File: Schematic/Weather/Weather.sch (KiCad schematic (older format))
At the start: 0 parts

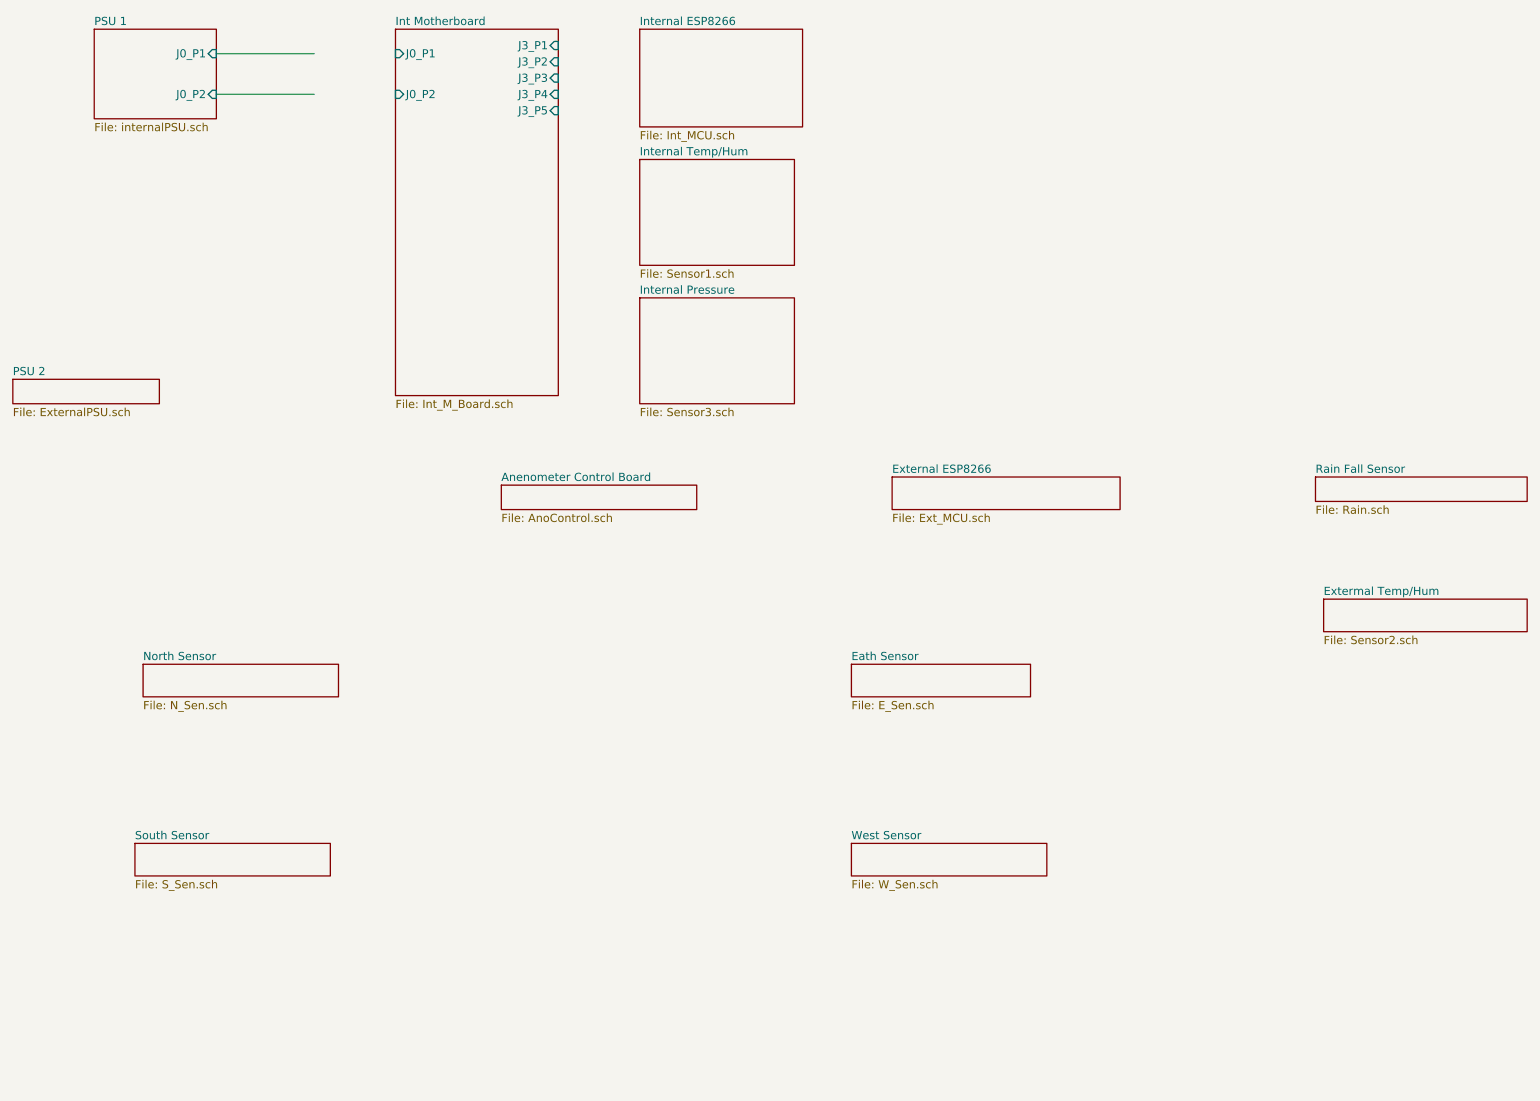
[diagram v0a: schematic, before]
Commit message: config connectors sda scl
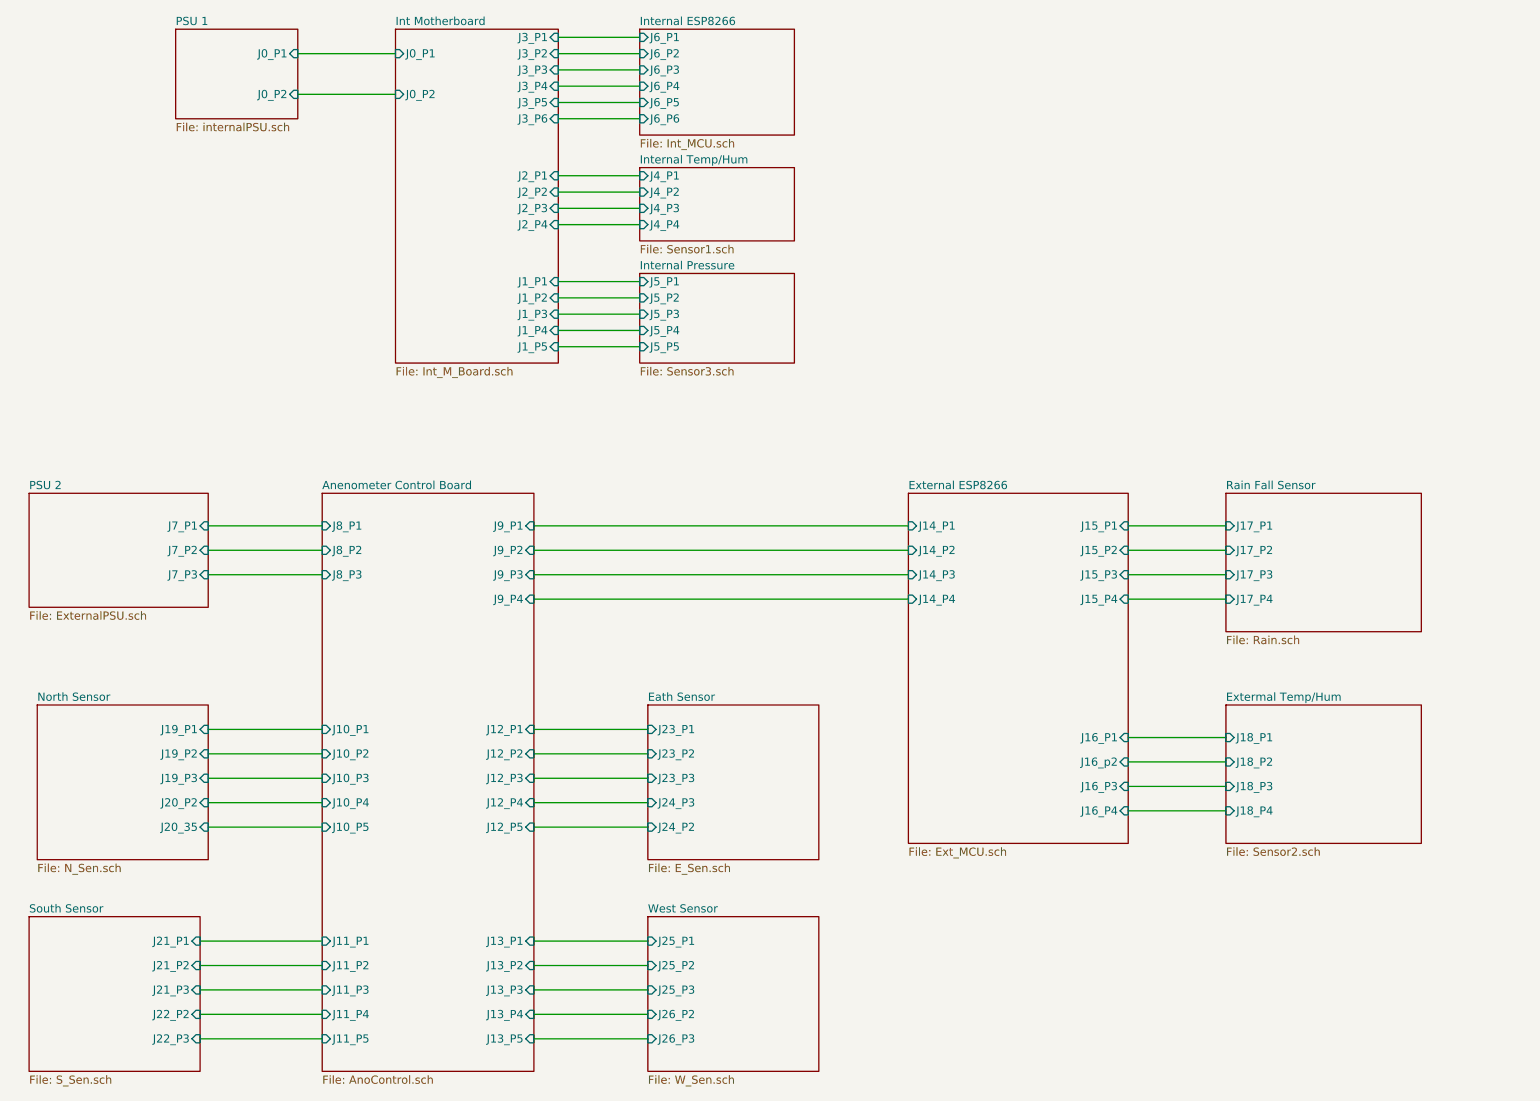
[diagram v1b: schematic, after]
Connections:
- wire segments 2 -> 52
